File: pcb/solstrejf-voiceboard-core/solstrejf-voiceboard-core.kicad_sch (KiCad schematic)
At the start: 35 parts, among them J1 Conn_02x05_Odd_Even, J2 Conn_02x08_Odd_Even, J3 Direct_Out, U1 AS3372E, U4 TL072

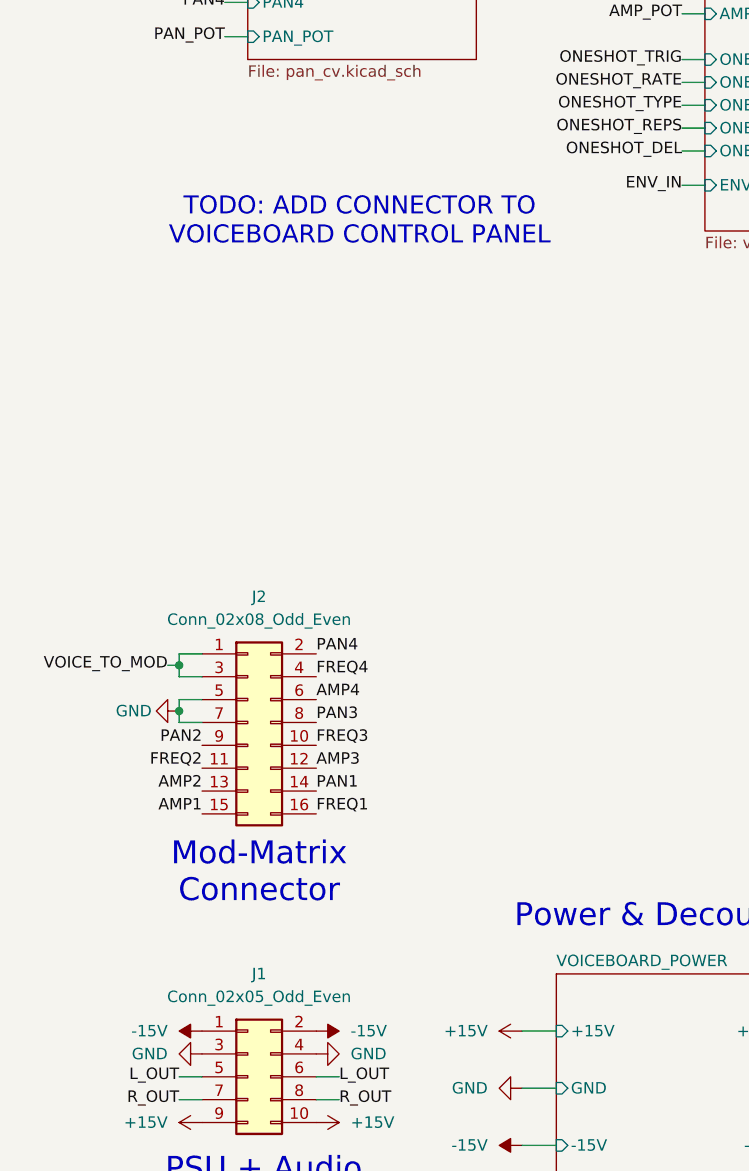
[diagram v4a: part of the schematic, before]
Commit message: Updated frequency CV summer circuit to use +/-12V local regulator instead of +/15V. Updated LTspice, notebooks, and KiCad project
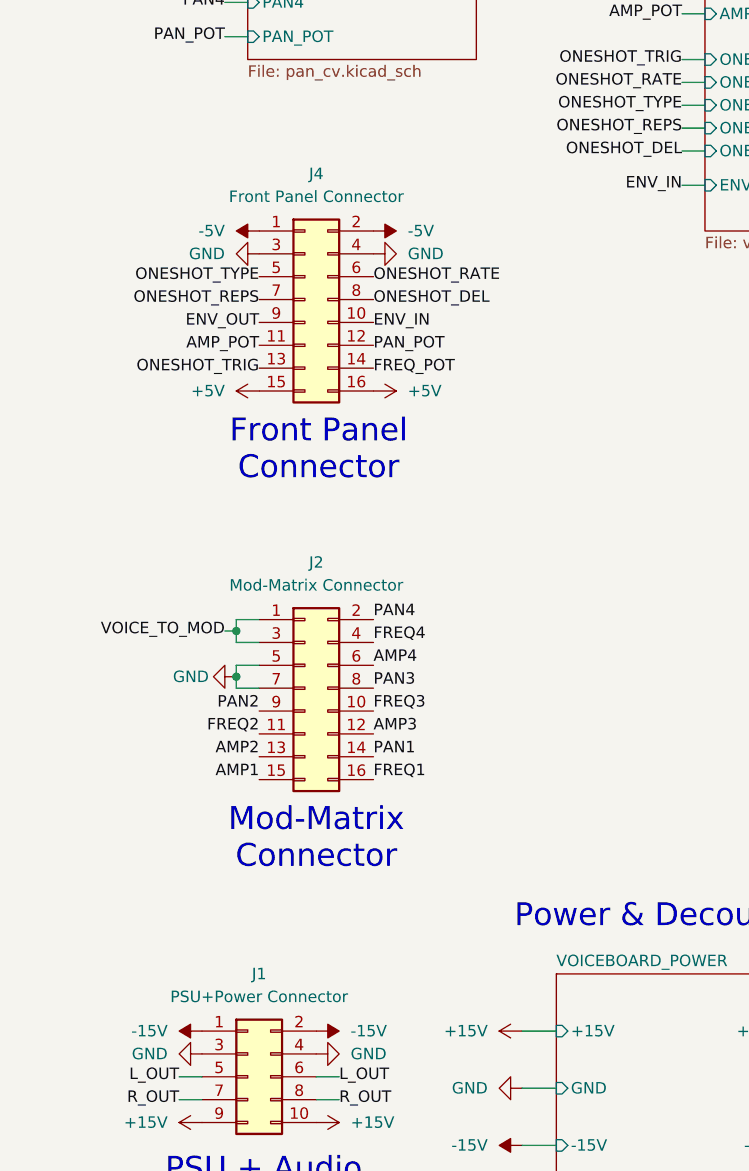
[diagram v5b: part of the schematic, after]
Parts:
- added J4: Front Panel Connector, Connector_IDC:IDC-Header_2x08_P2.54mm_Vertical, symbol Connector_Generic:Conn_02x08_Odd_Even
- J1: value Conn_02x05_Odd_Even -> PSU+Power Connector
- J2: value Conn_02x08_Odd_Even -> Mod-Matrix Connector
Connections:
- net +5V: now also J4.15 (Pin_15), J4.16 (Pin_16)
- net -5V: now also J4.1 (Pin_1), J4.2 (Pin_2)
- net AMP_POT: now also J4.11 (Pin_11)
- net ENV_IN: now also J4.10 (Pin_10)
- net ENV_OUT: now also J4.9 (Pin_9)
- net FREQ_POT: now also J4.14 (Pin_14)
- net GND: now also J4.3 (Pin_3), J4.4 (Pin_4)
- net ONESHOT_DEL: now also J4.8 (Pin_8)
- net ONESHOT_RATE: now also J4.6 (Pin_6)
- net ONESHOT_REPS: now also J4.7 (Pin_7)
- net ONESHOT_TRIG: now also J4.13 (Pin_13)
- net ONESHOT_TYPE: now also J4.5 (Pin_5)
- net PAN_POT: now also J4.12 (Pin_12)
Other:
- note added: "Front Panel Connector"
- note removed: "TODO: ADD CONNECTOR TO VOICEBOARD CONTROL PANEL"
- moved on the sheet: J2

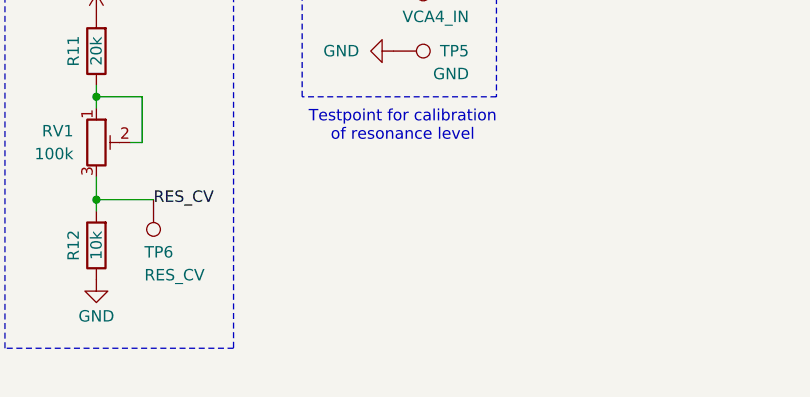
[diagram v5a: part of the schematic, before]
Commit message: Added M3 mounting holes to schematic/PCB and worked on power/regulator layout
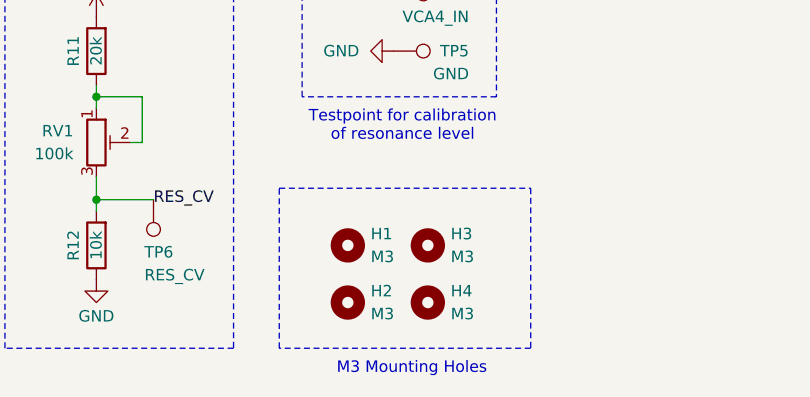
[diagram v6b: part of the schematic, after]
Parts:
- added H1, H2, H3, H4: M3, MountingHole:MountingHole_3.2mm_M3_DIN965, symbol Mechanical:MountingHole
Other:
- note added: "M3 Mounting Holes"
